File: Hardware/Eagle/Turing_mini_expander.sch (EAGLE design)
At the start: 20 parts, among them U1 TL072_

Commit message: Thonkiconn error corrected and re-routed
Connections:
- net GND: now also MAIN_OUT.SLEEVE; no longer MAIN_OUT.5
- net N$5: now also MAIN_OUT.TIP; no longer MAIN_OUT.3
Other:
- moved on the sheet: MAIN_OUT
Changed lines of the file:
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@@
 <?xml version="1.0" encoding="utf-8"?>
 <!DOCTYPE eagle SYSTEM "eagle.dtd">
-<eagle version="6.6.0">
+<eagle version="7.2.0">
 <drawing>
 <settings>
@@
 <net name="GND" class="2">
 <segment>
-<pinref part="MAIN_OUT" gate="G$1" pin="5"/>
+<pinref part="MAIN_OUT" gate="G$1" pin="SLEEVE"/>
 <pinref part="SUPPLY4" gate="GND" pin="GND"/>
 <wire x1="187.96" y1="129.54" x2="187.96" y2="127" width="0.1524" layer="91"/>
@@
 <wire x1="170.18" y1="121.92" x2="170.18" y2="134.62" width="0.1524" layer="91"/>
 <pinref part="R10" gate="G$1" pin="1"/>
-<pinref part="MAIN_OUT" gate="G$1" pin="3"/>
+<pinref part="MAIN_OUT" gate="G$1" pin="TIP"/>
 <wire x1="187.96" y1="134.62" x2="170.18" y2="134.62" width="0.1524" layer="91"/>
 <junction x="170.18" y="134.62"/>

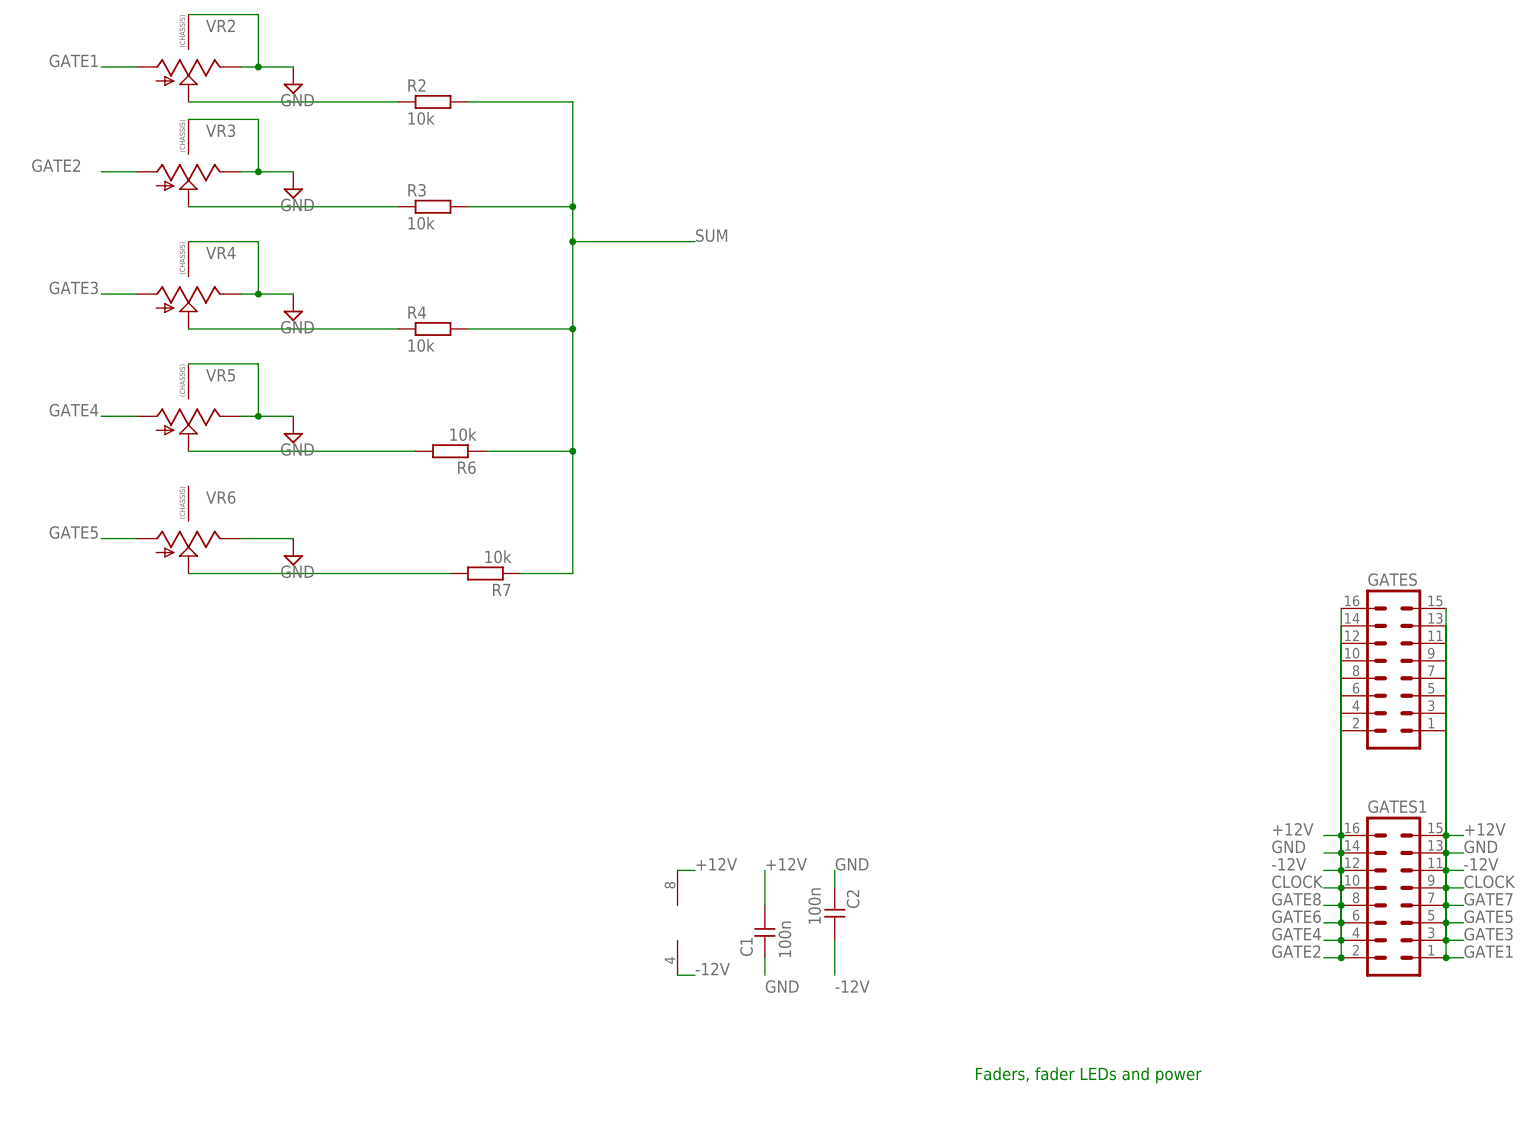
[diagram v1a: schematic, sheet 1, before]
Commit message: Fixes after first photo
Fixes #2, fixes #3, fixes #4
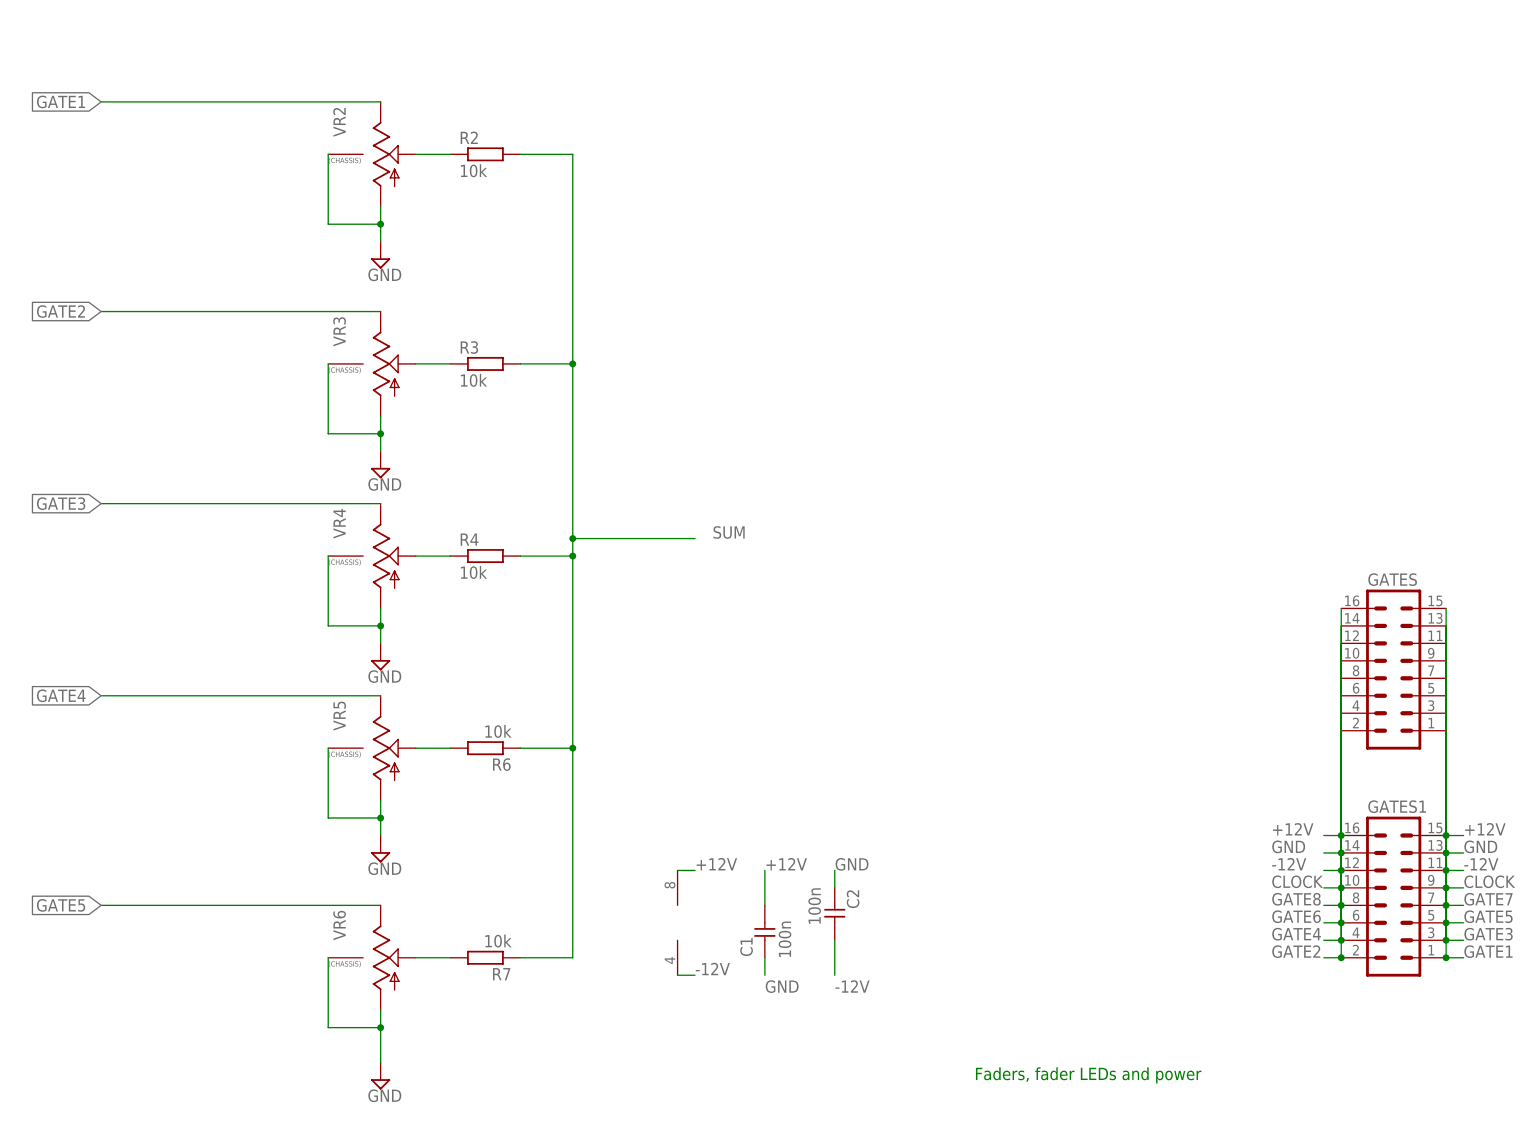
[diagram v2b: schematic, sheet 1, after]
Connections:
- net GATE1: now also VR2.E; no longer VR2.A
- net GATE2: now also VR3.E; no longer VR3.A
- net GATE3: now also VR4.E; no longer VR4.A
- net GATE4: now also VR5.E; no longer VR5.A
- net GATE5: now also VR6.E; no longer VR6.A
- net GND: now also VR2.A, VR3.A, VR4.A, VR5.A, VR6.A, VR6.P$1; no longer VR2.E, VR3.E, VR4.E, VR5.E, VR6.E
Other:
- moved on the sheet: R2, R3, R4, R6, R7, VR2, VR3, VR4, VR5, VR6

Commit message: Merge remote-tracking branch 'origin/master'
Conflicts:
	Hardware/Eagle/Turing_mini_expander.brd
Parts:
- R1: value 10k -> 2k
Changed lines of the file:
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@@
 <part name="VR5" library="MusicThingModular" deviceset="9MM_SNAP-IN_POT_CHASSIS" device=""/>
 <part name="VR6" library="MusicThingModular" deviceset="9MM_SNAP-IN_POT_CHASSIS" device=""/>
-<part name="R1" library="MusicThingModular" deviceset="RESISTOR" device="7MM" value="10k"/>
+<part name="R1" library="MusicThingModular" deviceset="RESISTOR" device="7MM" value="2k"/>
 <part name="R2" library="MusicThingModular" deviceset="RESISTOR" device="7MM" value="10k"/>
 <part name="R3" library="MusicThingModular" deviceset="RESISTOR" device="7MM" value="10k"/>

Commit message: Revert "Merge remote-tracking branch 'origin/master'"
This reverts commit c677e9c759e717a54841b66673ad6128330ede4f.
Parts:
- R1: value 2k -> 10k
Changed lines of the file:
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@@
 <part name="VR5" library="MusicThingModular" deviceset="9MM_SNAP-IN_POT_CHASSIS" device=""/>
 <part name="VR6" library="MusicThingModular" deviceset="9MM_SNAP-IN_POT_CHASSIS" device=""/>
-<part name="R1" library="MusicThingModular" deviceset="RESISTOR" device="7MM" value="2k"/>
+<part name="R1" library="MusicThingModular" deviceset="RESISTOR" device="7MM" value="10k"/>
 <part name="R2" library="MusicThingModular" deviceset="RESISTOR" device="7MM" value="10k"/>
 <part name="R3" library="MusicThingModular" deviceset="RESISTOR" device="7MM" value="10k"/>
